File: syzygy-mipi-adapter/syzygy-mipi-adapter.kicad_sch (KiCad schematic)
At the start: 96 parts, among them J1 Conn_02x06_Odd_Even, J2 SYZYGY_STD, J3 USB_C_Receptacle_USB2.0_16P, J4 SM03B-SRSS-TB, J6 501951-2230, J7 501951-2230, J8 501951-2230, Q1 DMG1024UV-7, Q2 DMG1024UV-7, U1 RP2350_80QFN, U10 PUSB3F96, U11 NCP115AMX330TCG, U2 W25Q32JVSSIQ, U3 PUSB3F96, U4 PUSB3F96, U5 PUSB3F96, U6 PUSB3F96, U7 PUSB3F96, U8 PUSB3F96, U9 PUSB3F96, Y1 ABM8-272-T3

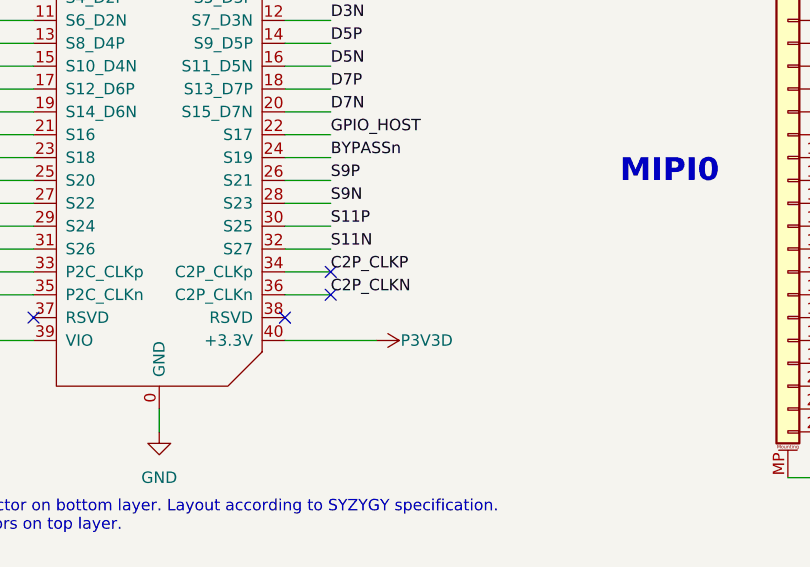
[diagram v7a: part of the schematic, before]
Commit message: Added test points for otherwise unconnected Syzygy pins
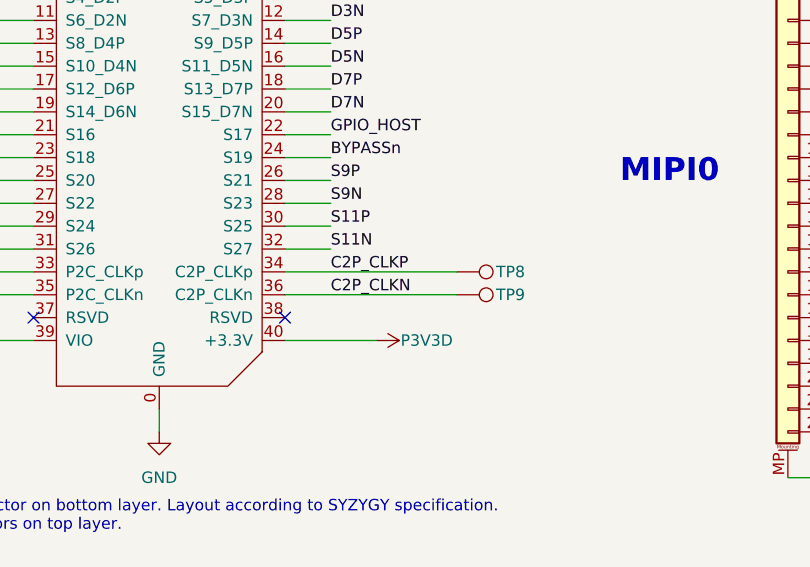
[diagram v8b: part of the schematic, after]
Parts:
- added TP8, TP9: TestPoint, TestPoint:TestPoint_Pad_1.0x1.0mm, symbol Connector:TestPoint
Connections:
- net C2P_CLKN: now also TP9.1
- net C2P_CLKP: now also TP8.1
- no-connect marks 36 -> 34
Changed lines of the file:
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@@
 	)
 	(no_connect
-		(at 320.04 107.95)
-	)
-	(no_connect
 		(at 153.67 207.01)
 	)
@@
 	)
 	(no_connect
-		(at 320.04 105.41)
-	)
-	(no_connect
 		(at 375.92 102.87)
 	)
@@
 	(wire
 		(pts
-			(xy 314.96 107.95) (xy 320.04 107.95)
+			(xy 314.96 107.95) (xy 334.01 107.95)
 		)
 		(stroke
@@
 	(wire
 		(pts
-			(xy 314.96 105.41) (xy 320.04 105.41)
+			(xy 314.96 105.41) (xy 334.01 105.41)
 		)
 		(stroke
@@
 	)
 	(symbol
+		(lib_id "Connector:TestPoint")
+		(at 334.01 107.95 270)
+		(unit 1)
+		(exclude_from_sim no)
+		(in_bom yes)
+		(on_board yes)
+		(dnp no)
+		(property "Reference" "TP9"
+			(at 341.63 107.95 90)
+			(effects
+				(font
+					(size 1.27 1.27)
+				)
+				(justify right)
+			)
+		)
+		(property "Value" "TestPoint"
+			(at 338.5819 105.41 0)
+			(effects
+				(font
+					(size 1.27 1.27)
+				)
+				(justify right)
+				(hide yes)
+			)
+		)
+		(property "Footprint" "TestPoint:TestPoint_Pad_1.0x1.0mm"
+			(at 334.01 113.03 0)
+			(effects
+				(font
+					(size 1.27 1.27)
+				)
+				(hide yes)
+			)
+		)
+		(property "Datasheet" "~"
+			(at 334.01 113.03 0)
+			(effects
+				(font
+					(size 1.27 1.27)
+				)
+				(hide yes)
+			)
+		)
+		(property "Description" "test point"
+			(at 334.01 107.95 0)
+			(effects
+				(font
+					(size 1.27 1.27)
+				)
+				(hide yes)
+			)
+		)
+		(pin "1"
+		)
+		(instances
+			(project "syzygy-mipi-adapter"
+				(path "/b75d5d5b-a423-49b6-bf7a-b3510d05dcb9"
+					(reference "TP9")
+					(unit 1)
+				)
+			)
+		)
+	)
+	(symbol
 		(lib_id "power:GND")
 		(at 165.1 194.31 270)
@@
 					(unit 1)
 				)
+			)
+		)
+	)
+	(symbol
+		(lib_id "Connector:TestPoint")
+		(at 334.01 105.41 270)
+		(unit 1)
+		(exclude_from_sim no)
+		(in_bom yes)
+		(on_board yes)
+		(dnp no)
+		(property "Reference" "TP8"
+			(at 341.63 105.41 90)
+			(effects
+				(font
+					(size 1.27 1.27)
+				)
+				(justify right)
+			)
+		)
+		(property "Value" "TestPoint"
+			(at 338.5819 102.87 0)
+			(effects
+				(font
+					(size 1.27 1.27)
+				)
+				(justify right)
+				(hide yes)
+			)
+		)
+		(property "Footprint" "TestPoint:TestPoint_Pad_1.0x1.0mm"
+			(at 334.01 110.49 0)
+			(effects
+				(font
+					(size 1.27 1.27)
+				)
+				(hide yes)
+			)
+		)
+		(property "Datasheet" "~"
+			(at 334.01 110.49 0)
+			(effects
+				(font
+					(size 1.27 1.27)
+				)
+				(hide yes)
+			)
+		)
+		(property "Description" "test point"
+			(at 334.01 105.41 0)
+			(effects
+				(font
+					(size 1.27 1.27)
+				)
+				(hide yes)
+			)
+		)
+		(pin "1"
+		)
+		(instances
+			(project "syzygy-mipi-adapter"
+				(path "/b75d5d5b-a423-49b6-bf7a-b3510d05dcb9"
+					(reference "TP8")
+					(unit 1)
+				)
